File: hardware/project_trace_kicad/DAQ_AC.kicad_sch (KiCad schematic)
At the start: 61 parts, among them U302 MCP6499T, U303 ADS1602, U304 LM4040DBZ-4.1, U306 ADA4950-1

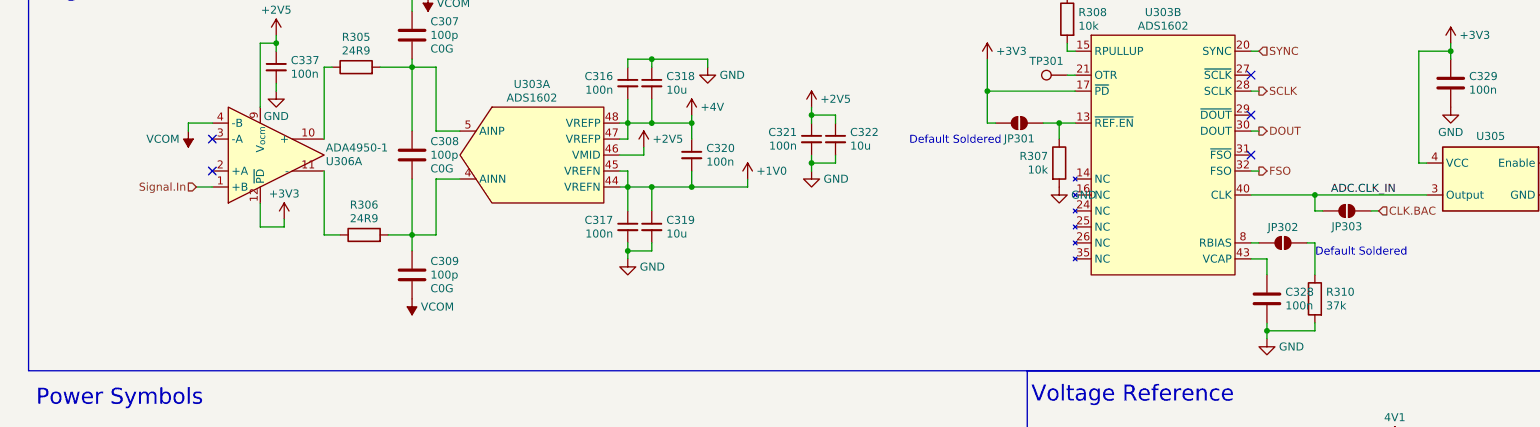
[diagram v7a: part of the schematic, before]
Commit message: Adjust Layer Thickness, fix insignificant DRC Warnings
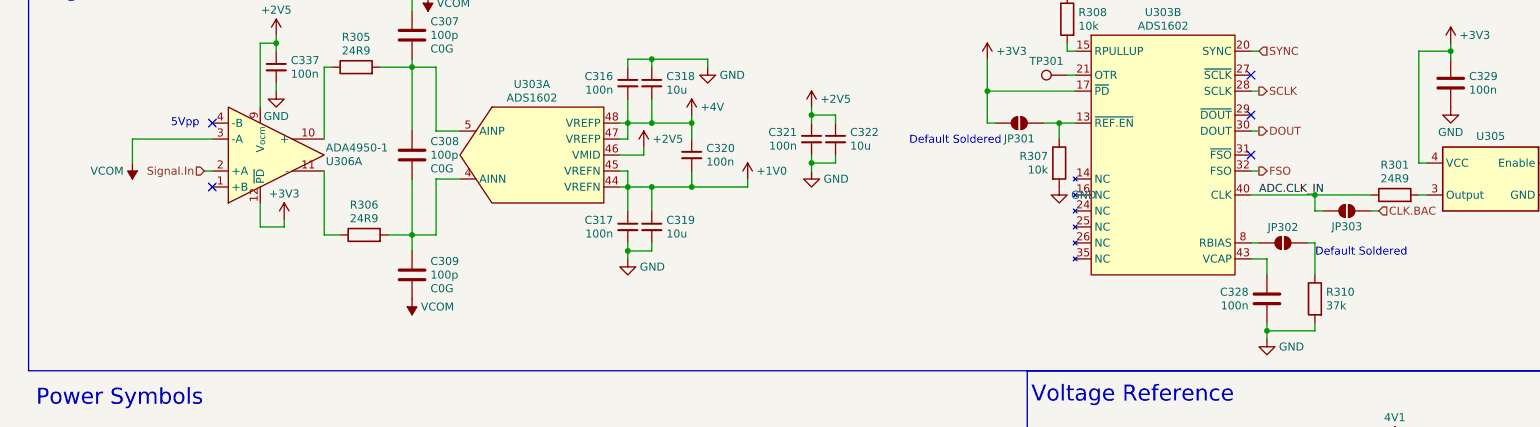
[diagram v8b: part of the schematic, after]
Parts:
- added R301: 24R9, Resistor_SMD:R_0603_1608Metric_Pad0.98x0.95mm_HandSolder, symbol Device:R
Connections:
- net ADC.CLK_IN: now also R301.1; no longer U305.3 (Output)
- net Signal.In: now also U306.2 (+A); no longer U306.1 (+B)
- net VCOM: now also U306.3 (-A); no longer U306.4 (-B)
- new net: R301.2, U305.3 (Output)
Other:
- note added: "5Vpp"
- moved on the sheet: C328
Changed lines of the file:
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@@
 		)
 	)
+	(text "5Vpp"
+		(exclude_from_sim no)
+		(at 43.942 43.18 0)
+		(effects
+			(font
+				(size 1.27 1.27)
+			)
+		)
+	)
 	(text "Default Soldered"
 		(exclude_from_sim no)
@@
 	)
 	(no_connect
-		(at 48.26 50.8)
+		(at 213.36 48.26)
 	)
 	(no_connect
-		(at 48.26 45.72)
+		(at 213.36 41.91)
 	)
 	(no_connect
-		(at 213.36 48.26)
+		(at 48.26 43.18)
 	)
 	(no_connect
-		(at 213.36 41.91)
+		(at 48.26 53.34)
 	)
 	(no_connect
@@
 	(wire
 		(pts
-			(xy 45.72 53.34) (xy 48.26 53.34)
+			(xy 46.99 50.8) (xy 48.26 50.8)
 		)
 		(stroke
@@
 	(wire
 		(pts
-			(xy 213.36 54.61) (xy 223.52 54.61)
+			(xy 213.36 54.61) (xy 232.41 54.61)
 		)
 		(stroke
@@
 	(wire
 		(pts
-			(xy 44.45 43.18) (xy 48.26 43.18)
+			(xy 35.56 45.72) (xy 48.26 45.72)
 		)
 		(stroke
@@
 	(wire
 		(pts
-			(xy 223.52 54.61) (xy 241.3 54.61)
+			(xy 215.9 64.77) (xy 213.36 64.77)
 		)
 		(stroke
@@
 	(wire
 		(pts
-			(xy 215.9 64.77) (xy 213.36 64.77)
+			(xy 236.22 93.98) (xy 236.22 95.25)
 		)
 		(stroke
@@
 	(wire
 		(pts
-			(xy 236.22 93.98) (xy 236.22 95.25)
+			(xy 111.76 120.65) (xy 110.49 120.65)
 		)
 		(stroke
@@
 	(wire
 		(pts
-			(xy 111.76 120.65) (xy 110.49 120.65)
+			(xy 143.51 49.53) (xy 147.32 49.53)
 		)
 		(stroke
@@
 	(wire
 		(pts
-			(xy 143.51 49.53) (xy 147.32 49.53)
+			(xy 55.88 104.14) (xy 55.88 102.87)
 		)
 		(stroke
@@
 	(wire
 		(pts
-			(xy 55.88 104.14) (xy 55.88 102.87)
+			(xy 59.69 59.69) (xy 55.88 59.69)
 		)
 		(stroke
@@
 	(wire
 		(pts
-			(xy 59.69 59.69) (xy 55.88 59.69)
+			(xy 240.03 54.61) (xy 241.3 54.61)
 		)
 		(stroke
@@
 	(wire
 		(pts
-			(xy 44.45 43.18) (xy 44.45 44.45)
+			(xy 35.56 45.72) (xy 35.56 49.53)
 		)
 		(stroke
@@
 	)
 	(label "ADC.CLK_IN"
-		(at 226.06 54.61 0)
+		(at 214.63 54.61 0)
 		(effects
 			(font
@@
 	(hierarchical_label "Signal.In"
 		(shape input)
-		(at 45.72 53.34 180)
+		(at 46.99 50.8 180)
 		(effects
 			(font
@@
 	(symbol
 		(lib_id "power:VCOM")
-		(at 44.45 44.45 0)
+		(at 35.56 49.53 0)
 		(mirror x)
 		(unit 1)
@@
 		(dnp no)
 		(property "Reference" "#PWR0301"
-			(at 44.45 40.64 0)
+			(at 35.56 45.72 0)
 			(hide yes)
 			(show_name no)
@@
 		)
 		(property "Value" "VCOM"
-			(at 43.053 45.72 0)
+			(at 34.163 50.8 0)
 			(show_name no)
 			(do_not_autoplace no)
@@
 		)
 		(property "Footprint" ""
-			(at 44.45 44.45 0)
+			(at 35.56 49.53 0)
 			(hide yes)
 			(show_name no)
@@
 		)
 		(property "Datasheet" ""
-			(at 44.45 44.45 0)
+			(at 35.56 49.53 0)
 			(hide yes)
 			(show_name no)
@@
 		)
 		(property "Description" "Power symbol creates a global label with name \"VCOM\""
-			(at 44.45 44.45 0)
+			(at 35.56 49.53 0)
 			(hide yes)
 			(show_name no)
@@
 	)
 	(symbol
+		(lib_id "Device:R")
+		(at 236.22 54.61 90)
+		(unit 1)
+		(body_style 1)
+		(exclude_from_sim no)
+		(in_bom yes)
+		(on_board yes)
+		(in_pos_files yes)
+		(dnp no)
+		(fields_autoplaced yes)
+		(property "Reference" "R301"
+			(at 236.22 49.8346 90)
+			(show_name no)
+			(do_not_autoplace no)
+			(effects
+				(font
+					(size 1.27 1.27)
+				)
+			)
+		)
+		(property "Value" "24R9"
+			(at 236.22 52.0022 90)
+			(show_name no)
+			(do_not_autoplace no)
+			(effects
+				(font
+					(size 1.27 1.27)
+				)
+			)
+		)
+		(property "Footprint" "Resistor_SMD:R_0603_1608Metric_Pad0.98x0.95mm_HandSolder"
+			(at 236.22 56.388 90)
+			(hide yes)
+			(show_name no)
+			(do_not_autoplace no)
+			(effects
+				(font
+					(size 1.27 1.27)
+				)
+			)
+		)
+		(property "Datasheet" ""
+			(at 236.22 54.61 0)
+			(hide yes)
+			(show_name no)
+			(do_not_autoplace no)
+			(effects
+				(font
+					(size 1.27 1.27)
+				)
+			)
+		)
+		(property "Description" "Resistor"
+			(at 236.22 54.61 0)
+			(hide yes)
+			(show_name no)
+			(do_not_autoplace no)
+			(effects
+				(font
+					(size 1.27 1.27)
+				)
+			)
+		)
+		(property "DigikeyPN" "YAG4511CT-ND"
+			(at 236.22 54.61 90)
+			(hide yes)
+			(show_name no)
+			(do_not_autoplace no)
+			(effects
+				(font
+					(size 1.27 1.27)
+				)
+			)
+		)
+		(property "DIgikeyPN" ""
+			(at 236.22 54.61 90)
+			(hide yes)
+			(show_name no)
+			(do_not_autoplace no)
+			(effects
+				(font
+					(size 1.27 1.27)
+				)
+			)
+		)
+		(pin "1"
+		)
+		(pin "2"
+		)
+		(instances
+			(project "project_trace_kicad"
+				(path "/af51f4e5-b952-4b0e-baf2-78a72fb86fcd/ac2add4a-2a5e-456c-897d-914b794115d5"
+					(reference "R301")
+					(unit 1)
+				)
+			)
+		)
+	)
+	(symbol
 		(lib_id "power:+4V")
 		(at 261.62 99.06 0)
@@
 	(symbol
 		(lib_id "Device:C")
-		(at 215.9 71.12 180)
+		(at 215.9 71.12 0)
+		(mirror x)
 		(unit 1)
 		(body_style 1)
@@
 		(in_pos_files yes)
 		(dnp no)
-		(fields_autoplaced yes)
 		(property "Reference" "C328"
-			(at 218.821 70.0362 0)
+			(at 212.979 70.0362 0)
 			(show_name no)
 			(do_not_autoplace no)
@@
 		)
 		(property "Value" "100n"
-			(at 218.821 72.2038 0)
+			(at 212.979 72.2038 0)
 			(show_name no)
 			(do_not_autoplace no)
@@
 		)
 		(property "Footprint" "Capacitor_SMD:C_0603_1608Metric_Pad1.08x0.95mm_HandSolder"
-			(at 214.9348 67.31 0)
+			(at 216.8652 67.31 0)
 			(hide yes)
 			(show_name no)
